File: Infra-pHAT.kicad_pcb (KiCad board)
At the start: 2 copper layers, 0 parts

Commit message: made the pcb template based on the Pi zero footprint
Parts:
- added RASP_CONN1: Raspberry_PI, Pin_Headers:Pin_Header_Straight_2x20, F.Cu at (156.8, 79.8)
- added REF1: MountingHole_2.7mm_M2.5_DIN965_Pad, Mounting_Holes:MountingHole_2.7mm_M2.5_DIN965_Pad, F.Cu at (152.0, 78.5)
- added REF2: MountingHole_2.7mm_M2.5_DIN965_Pad, Mounting_Holes:MountingHole_2.7mm_M2.5_DIN965_Pad, F.Cu at (210.0, 78.5)
- added REF3: MountingHole_2.7mm_M2.5_DIN965_Pad, Mounting_Holes:MountingHole_2.7mm_M2.5_DIN965_Pad, F.Cu at (210.0, 101.5)
- added REF4: MountingHole_2.7mm_M2.5_DIN965_Pad, Mounting_Holes:MountingHole_2.7mm_M2.5_DIN965_Pad, F.Cu at (152.0, 101.5)
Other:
- board outline added: 65 x 30 mm

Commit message: Placed Connectors for: UART + IRTX
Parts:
- added IRRX: TSOP34838, myfootprint:TSOP38X, F.Cu at (166.8, 99.7)
- added IRTX1: L-53F3BT, LEDs:LED-5MM, F.Cu at (152.8, 87.8)
- added IRTX2: L-53F3BT, LEDs:LED-5MM, F.Cu at (152.8, 95.4)
- added Q1: BC817, TO_SOT_Packages_SMD:SOT-23, F.Cu at (159.7, 86.6)
- added R4: 10K, Resistors_SMD:R_0603_HandSoldering, F.Cu at (159.6, 91.6)
- added REF**: FanPinHeader_1x04_P2.54mm_Vertical, Connector:FanPinHeader_1x04_P2.54mm_Vertical, F.Cu at (185.4, 97.8)
- added UART: CONN_01X04, Pin_Headers:Pin_Header_Straight_1x04, F.Cu at (167.1, 86.5)
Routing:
- net /RXD: track 0.30 -> 0.87 mm
- added copper zone on B.Cu, net GND
- added copper zone on F.Cu, net GND
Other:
- board text added: "10K"
- board text added: "BC817"

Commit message: Updated the I2C Connectors + Added Few Components
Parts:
- removed REF**: FanPinHeader_1x04_P2.54mm_Vertical, Connector:FanPinHeader_1x04_P2.54mm_Vertical
- added C2: 4.7, Capacitors_SMD:C_0805_HandSoldering, F.Cu at (168.1, 96.6)
- added R5: 470, Resistors_SMD:R_0603_HandSoldering, F.Cu at (169.3, 91.6)
- added R6: 4.7K, Resistors_SMD:R_0603_HandSoldering, F.Cu at (174.4, 91.6)
- added R7: 4.7K, Resistors_SMD:R_0603_HandSoldering, F.Cu at (174.4, 96.6)
- added SENS1: I2C_SENS_1, Pin_Headers:Pin_Header_Straight_1x04, F.Cu at (188.4, 96.6)
- added SENS2: I2C_SENS_1, Pin_Headers:Pin_Header_Straight_1x04, F.Cu at (188.4, 91.6)
- added SENS3: I2C_SENS_1, Pin_Headers:Pin_Header_Straight_1x04, F.Cu at (188.4, 86.5)
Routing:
- net +3V3: track 0.60 -> 1.39 mm
- removed copper zone on B.Cu, net GND
- removed copper zone on F.Cu, net GND
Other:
- board text added: "3.3V TX RX GND"
- board text added: "3x I2C"
- board text added: "4,7K"
- board text added: "4,7pF"
- board text added: "470"
- board text added: "SDA SCL GND 3.3V"

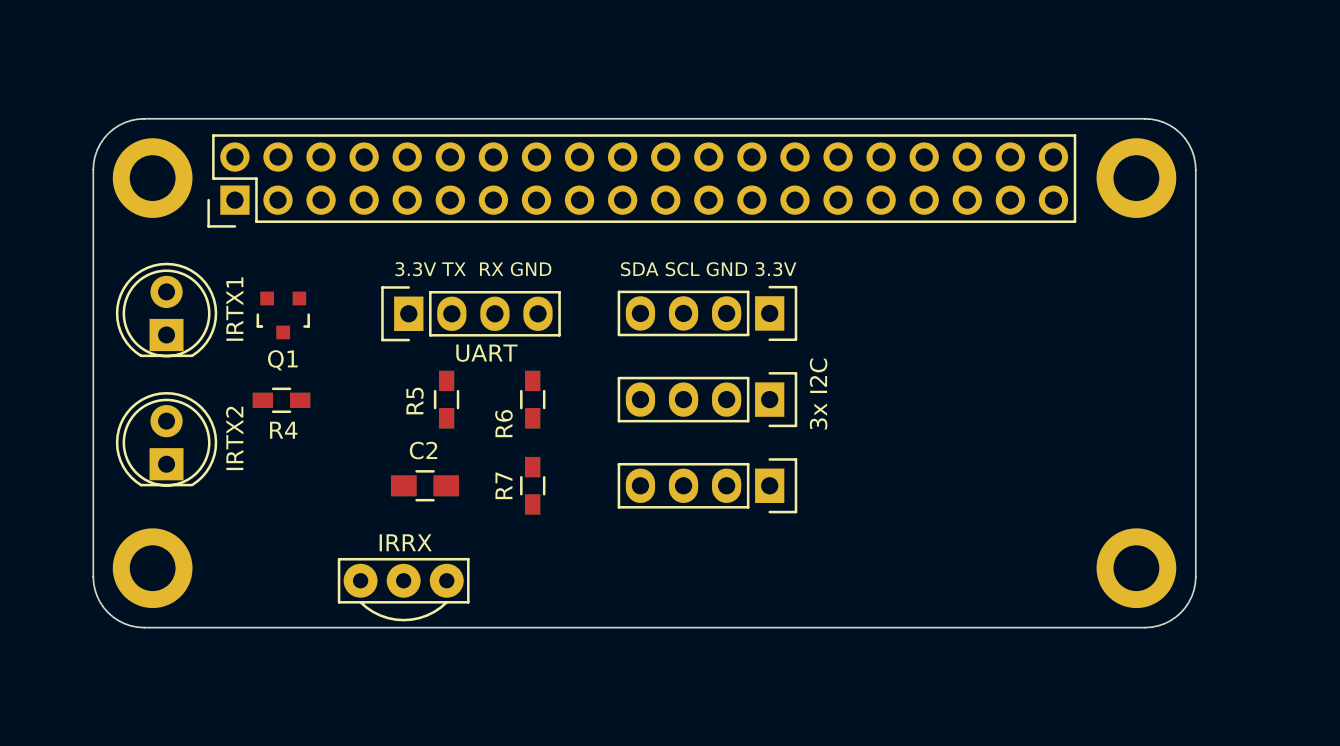
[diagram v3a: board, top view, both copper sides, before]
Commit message: Added DIP8 Footprint for CAT24C32WI-GT3
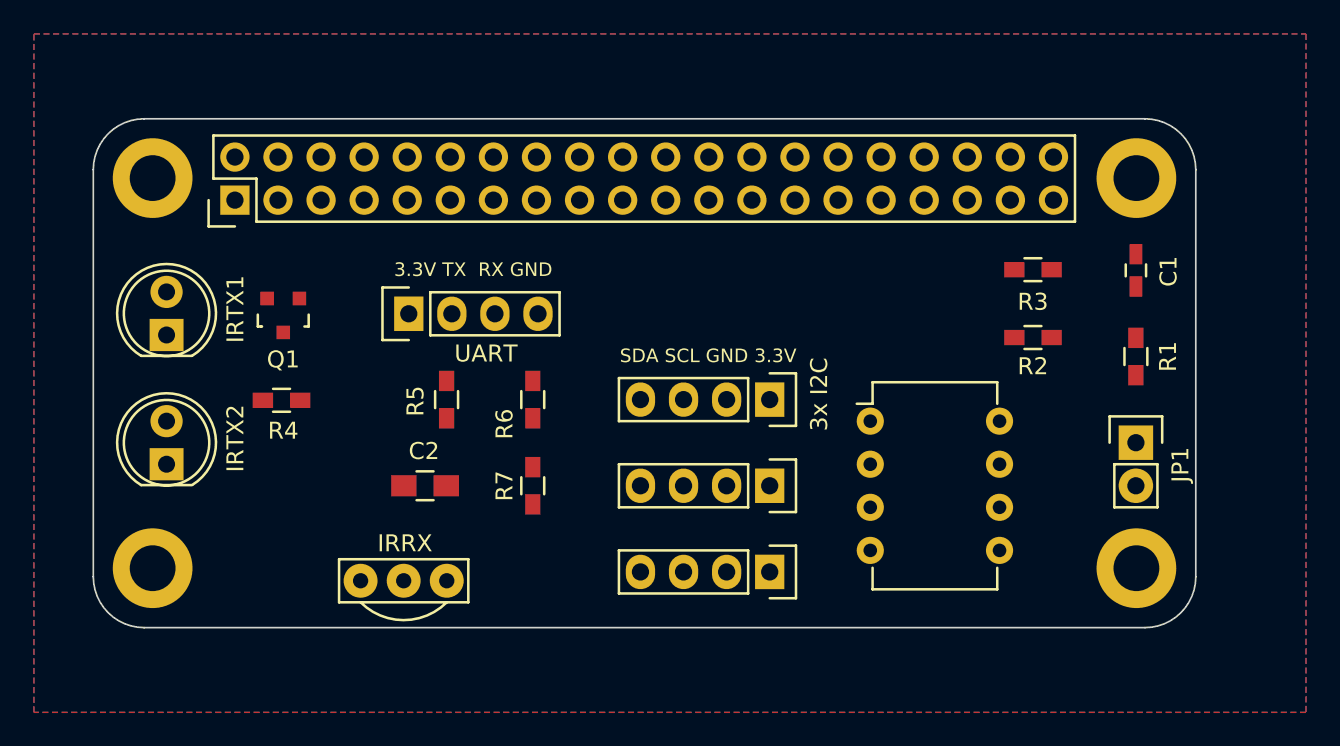
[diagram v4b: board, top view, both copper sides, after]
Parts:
- added C1: 0.1, Capacitors_SMD:C_0603_HandSoldering, F.Cu at (210.0, 83.9)
- added JP1: JUMPER, Pin_Headers:Pin_Header_Straight_1x02, F.Cu at (210.0, 94.1)
- added R1: 1K, Resistors_SMD:R_0603_HandSoldering, F.Cu at (210.0, 89.0)
- added R2: 4.7K, Resistors_SMD:R_0603_HandSoldering, F.Cu at (203.9, 87.9)
- added R3: 4.7K, Resistors_SMD:R_0603_HandSoldering, F.Cu at (203.9, 83.9)
- added U1: CAT24C32WI-GT3, Housings_DIP:DIP-8_W7.62mm, F.Cu at (194.3, 92.8)
- moved SENS1 5.08 mm to (188.4, 101.7)
- moved SENS2 5.08 mm to (188.4, 96.6)
- moved SENS3 5.08 mm to (188.4, 91.6)
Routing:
- added copper zone on B.Cu, net GND
- added copper zone on F.Cu, net GND
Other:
- board text added: "100nF"
- board text added: "1K"

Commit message: front copper layer routed
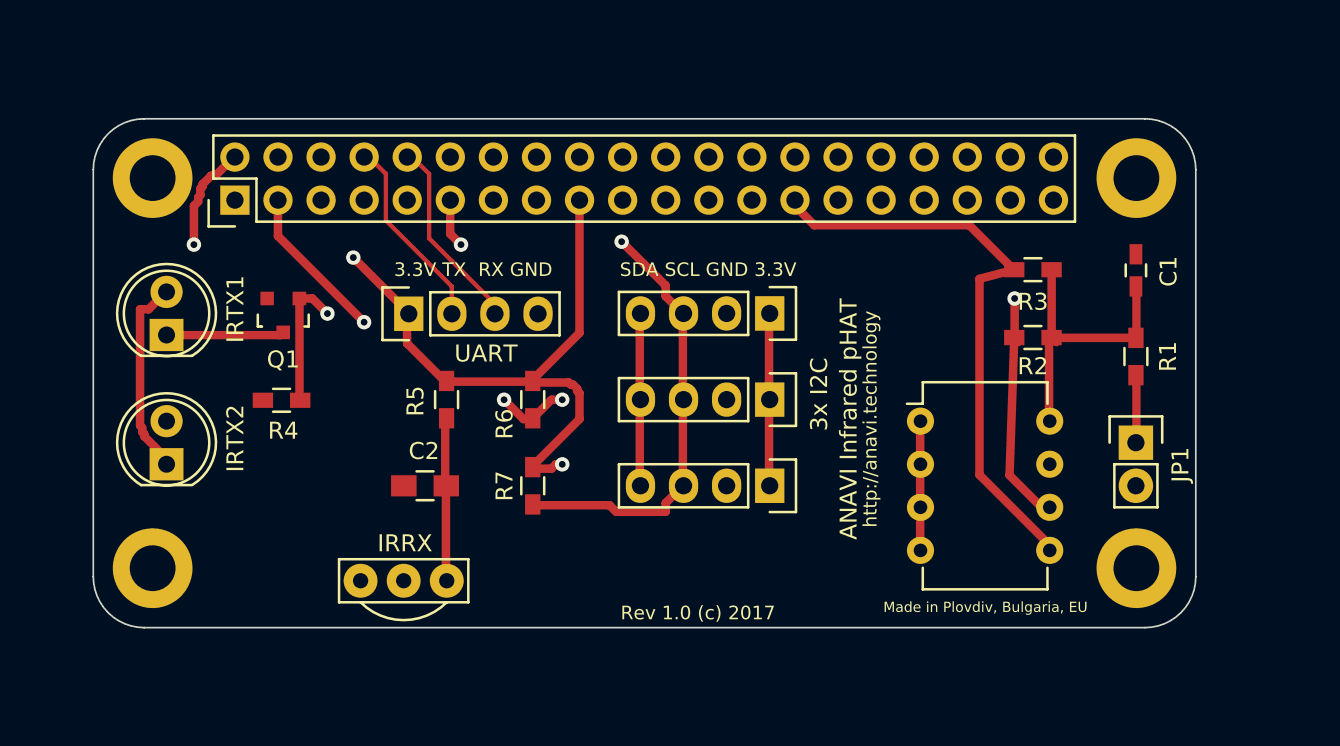
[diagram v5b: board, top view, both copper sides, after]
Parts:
- moved SENS1 5.08 mm to (188.4, 96.6)
- moved SENS2 5.08 mm to (188.4, 91.6)
- moved SENS3 5.08 mm to (188.4, 86.5)
- moved U1 2.96 mm to (197.3, 92.8)
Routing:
- net +3V3: track 1.39 -> 67.3 mm, vias 0 -> 2
- net Net-(R3-Pad2): track 0.43 -> 35.1 mm
- net Net-(R7-Pad2): track 0.28 -> 26.2 mm, vias 0 -> 1
- net Net-(R6-Pad2): track 0.24 -> 24.2 mm, vias 0 -> 3
- net Net-(R2-Pad2): track 0.04 -> 14.1 mm, vias 0 -> 1
- net Net-(IRTX1-Pad2): track 0.46 -> 11.8 mm
- net /TXD: track 0.29 -> 11.6 mm
- net Net-(Q1-Pad1): track 0.04 -> 11.1 mm, vias 0 -> 2
- net /RXD: track 0.87 -> 11.6 mm
- net Net-(C2-Pad1): track 0.09 -> 9.96 mm
- net GND: track 0.00 -> 8.40 mm
- net Net-(IRTX1-Pad1): track 0.04 -> 7.02 mm
- net +5V: track 0.08 -> 6.44 mm, vias 0 -> 1
- net Net-(JP1-Pad1): track 0.21 -> 4.50 mm
- removed copper zone on B.Cu, net GND
- removed copper zone on F.Cu, net GND
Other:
- board text added: "ANAVI Infrared pHAT"
- board text added: "Made in Plovdiv, Bulgaria, EU"
- board text added: "Rev 1.0 (c) 2017"
- board text added: "http://anavi.technology"

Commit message: back copper layer routed
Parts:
- added ?: LOGO, logo:anavi-logo, F.Cu at (175.2, 101.7)
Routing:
- net Net-(IRRX1-Pad1): track 0.26 -> 45.1 mm
- net +3V3: track 67.3 -> 105.5 mm
- net Net-(R2-Pad2): track 14.1 -> 42.8 mm
- net Net-(R7-Pad2): track 26.2 -> 45.2 mm
- net Net-(R6-Pad2): track 24.2 -> 39.0 mm
- net +5V: track 6.44 -> 17.5 mm
- net Net-(Q1-Pad1): track 11.1 -> 20.6 mm
- net Net-(JP1-Pad1): track 4.50 -> 10.1 mm
- added copper zone on B.Cu, net GND
- added copper zone on F.Cu, net GND

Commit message: deleted the front & back zones
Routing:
- removed copper zone on B.Cu, net GND
- removed copper zone on F.Cu, net GND
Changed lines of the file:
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@@
-(kicad_pcb (version 4) (host pcbnew 4.0.4+dfsg1-stable)
+(kicad_pcb (version 20171130) (host pcbnew "(5.1.5-0-10_14)")
   (general
-    (links 59)
-    (no_connects 2)
-    (area 136.817429 66.3 225.182572 110.000001)
     (thickness 1.6)
     (drawings 31)
@@
   )
   (layers
-    (0 F.Cu signal hide)
-    (31 B.Cu signal hide)
-    (32 B.Adhes user hide)
-    (33 F.Adhes user hide)
-    (34 B.Paste user hide)
-    (35 F.Paste user hide)
-    (36 B.SilkS user hide)
-    (37 F.SilkS user hide)
-    (38 B.Mask user hide)
-    (39 F.Mask user hide)
-    (40 Dwgs.User user hide)
-    (41 Cmts.User user hide)
-    (42 Eco1.User user hide)
-    (43 Eco2.User user hide)
+    (0 F.Cu signal)
+    (31 B.Cu signal)
+    (32 B.Adhes user)
+    (33 F.Adhes user)
+    (34 B.Paste user)
+    (35 F.Paste user)
+    (36 B.SilkS user)
+    (37 F.SilkS user)
+    (38 B.Mask user)
+    (39 F.Mask user)
+    (40 Dwgs.User user)
+    (41 Cmts.User user)
+    (42 Eco1.User user)
+    (43 Eco2.User user)
     (44 Edge.Cuts user)
-    (45 Margin user hide)
-    (46 B.CrtYd user hide)
+    (45 Margin user)
+    (46 B.CrtYd user)
     (47 F.CrtYd user)
-    (48 B.Fab user hide)
+    (48 B.Fab user)
     (49 F.Fab user)
   )
@@
     (zone_45_only no)
     (trace_min 0.25)
-    (segment_width 0.2)
-    (edge_width 0.1)
     (via_size 0.85)
     (via_drill 0.4)
@@
     (uvia_min_size 0.2)
     (uvia_min_drill 0.1)
+    (edge_width 0.1)
+    (segment_width 0.2)
     (pcb_text_width 0.3)
     (pcb_text_size 1.5 1.5)
@@
       (layerselection 0x010e0_80000001)
       (usegerberextensions true)
+      (usegerberattributes false)
+      (usegerberadvancedattributes false)
+      (creategerberjobfile false)
       (excludeedgelayer true)
       (linewidth 0.100000)
@@
       (hpglpennumber 1)
       (hpglpenspeed 20)
-      (hpglpendiameter 15)
-      (hpglpenoverlay 2)
+      (hpglpendiameter 15.000000)
       (psnegative false)
       (psa4output false)
@@
       (drillshape 0)
       (scaleselection 1)
-      (outputdirectory schemes/))
+      (outputdirectory "schemes/"))
   )
   (net 0 "")
@@
       (net 4 "Net-(IRTX1-Pad2)"))
     (model LEDs.3dshapes/LED-5MM.wrl
-      (at (xyz 0.05 0 0))
+      (offset (xyz 1.269999980926514 0 0))
       (scale (xyz 1 1 1))
       (rotate (xyz 0 0 90))
@@
       (net 5 +5V))
     (model LEDs.3dshapes/LED-5MM.wrl
-      (at (xyz 0.05 0 0))
+      (offset (xyz 1.269999980926514 0 0))
       (scale (xyz 1 1 1))
       (rotate (xyz 0 0 90))
@@
       (net 2 GND))
     (model Pin_Headers.3dshapes/Pin_Header_Straight_1x02.wrl
-      (at (xyz 0 -0.05 0))
+      (offset (xyz 0 -1.269999980926514 0))
       (scale (xyz 1 1 1))
       (rotate (xyz 0 0 90))
@@
       (net 35 "Net-(RASP_CONN1-Pad40)"))
     (model Pin_Headers.3dshapes/Pin_Header_Straight_2x20.wrl
-      (at (xyz 0.05 -0.95 0))
+      (offset (xyz 1.269999980926514 -24.12999963760376 0))
       (scale (xyz 1 1 1))
       (rotate (xyz 0 0 90))
@@
       (net 10 "Net-(R6-Pad2)"))
     (model Pin_Headers.3dshapes/Pin_Header_Straight_1x04.wrl
-      (at (xyz 0 -0.15 0))
+      (offset (xyz 0 -3.809999942779541 0))
       (scale (xyz 1 1 1))
       (rotate (xyz 0 0 90))
@@
       (net 10 "Net-(R6-Pad2)"))
     (model Pin_Headers.3dshapes/Pin_Header_Straight_1x04.wrl
-      (at (xyz 0 -0.15 0))
+      (offset (xyz 0 -3.809999942779541 0))
       (scale (xyz 1 1 1))
       (rotate (xyz 0 0 90))
@@
       (net 10 "Net-(R6-Pad2)"))
     (model Pin_Headers.3dshapes/Pin_Header_Straight_1x04.wrl
-      (at (xyz 0 -0.15 0))
+      (offset (xyz 0 -3.809999942779541 0))
       (scale (xyz 1 1 1))
       (rotate (xyz 0 0 90))
@@
       (net 2 GND))
     (model Pin_Headers.3dshapes/Pin_Header_Straight_1x04.wrl
-      (at (xyz 0 -0.15 0))
+      (offset (xyz 0 -3.809999942779541 0))
       (scale (xyz 1 1 1))
       (rotate (xyz 0 0 90))
@@
     (at 175.2 101.7)
     (fp_text reference "" (at 0 0) (layer F.SilkS) hide
-      (effects (font (thickness 0.3)))
+      (effects (font (size 1.524 1.524) (thickness 0.3)))
     )
     (fp_text value LOGO (at 0.75 0) (layer F.SilkS) hide
-      (effects (font (thickness 0.3)))
+      (effects (font (size 1.524 1.524) (thickness 0.3)))
     )
     (fp_poly (pts (xy 1.693334 1.693334) (xy -1.693333 1.693334) (xy -1.693333 -1.524) (xy -1.185333 -1.524)
@@
   (segment (start 159.512 87.757) (end 152.781 87.757) (width 0.5) (layer F.Cu) (net 15) (status 80000))
   (segment (start 152.781 87.757) (end 152.82 87.75) (width 0.5) (layer F.Cu) (net 15) (status 80000))
-  (zone (net 2) (net_name GND) (layer F.Cu) (hatch edge 0.508)
-    (connect_pads (clearance 0.508))
-    (min_thickness 0.254)
-    (fill yes (arc_segments 16) (thermal_gap 0.508) (thermal_bridge_width 0.508))
-    (polygon
-      (pts
-        (xy 220 110) (xy 145 110) (xy 145 70) (xy 220 70)
-      )
-    )
-  )
-  (zone (net 2) (net_name GND) (layer B.Cu) (hatch edge 0.508)
-    (connect_pads (clearance 0.508))
-    (min_thickness 0.254)
-    (fill yes (arc_segments 16) (thermal_gap 0.508) (thermal_bridge_width 0.508))
-    (polygon
-      (pts
-        (xy 220 110) (xy 145 110) (xy 145 70) (xy 220 70)
-      )
-    )
-  )
 )
